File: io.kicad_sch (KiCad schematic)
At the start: 1 part, among them IC24 82C711

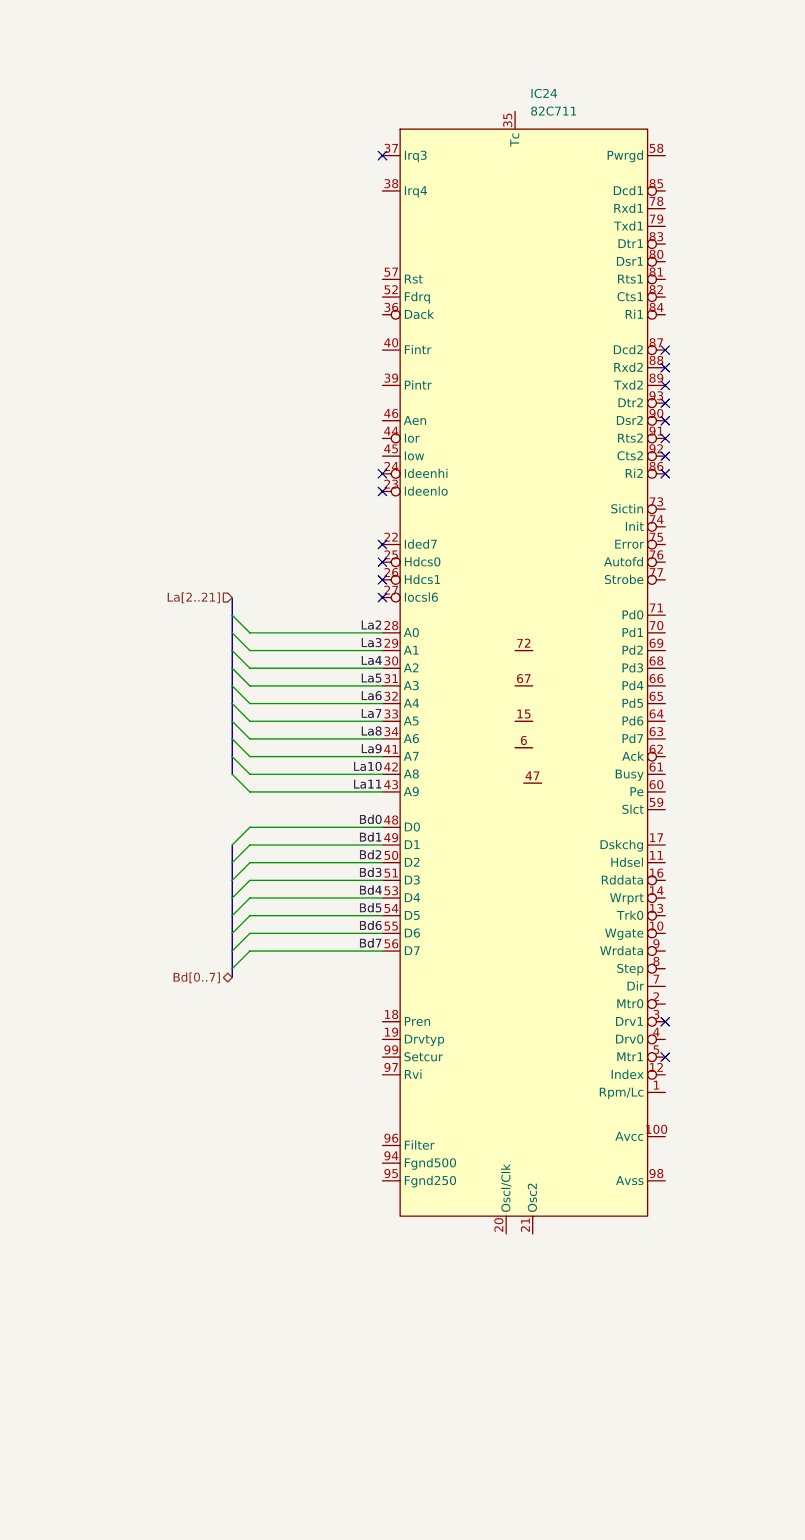
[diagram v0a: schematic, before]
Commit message: add io details
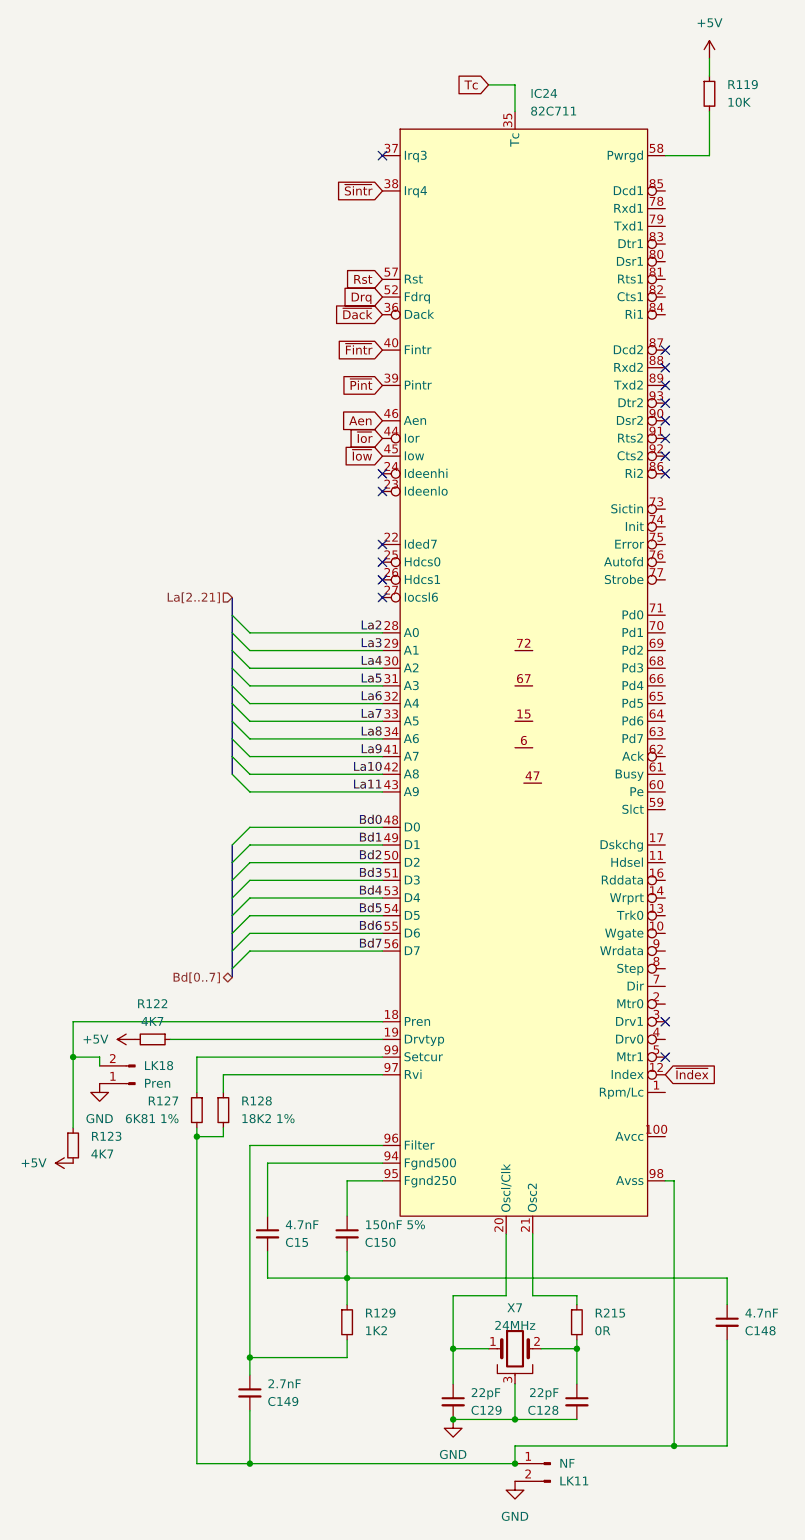
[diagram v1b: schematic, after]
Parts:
- added C128, C129: 22pF, Capacitor_SMD:C_0805_2012Metric, symbol Device:C_Small
- added C148, C15: 4.7nF, Capacitor_THT:C_Rect_L7.0mm_W2.5mm_P5.00mm, symbol Device:C_Small
- added C149: 2.7nF, Capacitor_SMD:C_0805_2012Metric, symbol Device:C_Small
- added C150: 150nF 5%, Capacitor_THT:C_Rect_L7.0mm_W2.5mm_P5.00mm, symbol Device:C_Small
- added LK11: NF, Connector_PinHeader_2.54mm:PinHeader_1x02_P2.54mm_Vertical, symbol Connector:Conn_01x02_Pin
- added LK18: Pren, Connector_PinHeader_2.54mm:PinHeader_1x02_P2.54mm_Vertical, symbol Connector:Conn_01x02_Pin
- added R119: 10K, Resistor_SMD:R_0805_2012Metric, symbol Device:R_Small
- added R122, R123: 4K7, Resistor_SMD:R_0805_2012Metric, symbol Device:R_Small
- added R127: 6K81 1%, Resistor_SMD:R_0805_2012Metric, symbol Device:R_Small
- added R128: 18K2 1%, Resistor_SMD:R_0805_2012Metric, symbol Device:R_Small
- added R129: 1K2, Resistor_SMD:R_0805_2012Metric, symbol Device:R_Small
- added R215: 0R, Resistor_SMD:R_0805_2012Metric, symbol Device:R_Small
- added X7: 24MHz, Crystal:Crystal_HC50_Horizontal_1EP_style2, symbol Device:Crystal_GND3
- IC24: footprint Package_QFP:TQFP-100_14x14mm_P0.5mm -> Package_QFP:PQFP-100_14x20mm_P0.65mm
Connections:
- net ~{Index}: now reaches IC24.12 (Index)
- net at IC24.18 (Pren): now also LK18.2 (Pin_2), R123.1
- net at IC24.19 (Drvtyp): now also R122.1
- net at IC24.20 (Oscl/Clk): now also C129.1, X7.1
- net at IC24.21 (Osc2): now also R215.1
- net Tc: now reaches IC24.35 (Tc)
- net ~{Dack}: now reaches IC24.36 (Dack)
- net ~{Sintr}: now reaches IC24.38 (Irq4)
- net ~{Pint}: now reaches IC24.39 (Pintr)
- net ~{Fintr}: now reaches IC24.40 (Fintr)
- net ~{Ior}: now reaches IC24.44 (Ior)
- net ~{Iow}: now reaches IC24.45 (Iow)
- net Aen: now reaches IC24.46 (Aen)
- net Drq: now reaches IC24.52 (Fdrq)
- net Rst: now reaches IC24.57 (Rst)
- net at IC24.58 (Pwrgd): now also R119.2
- net at IC24.94 (Fgnd500): now also C15.1
- net at IC24.95 (Fgnd250): now also C150.1
- net at IC24.96 (Filter): now also C149.1, R129.2
- net at IC24.97 (Rvi): now also R128.1
- net at IC24.98 (Avss): now also C148.2, C149.2, LK11.1 (Pin_1), R127.2, R128.2
- net at IC24.99 (Setcur): now also R127.1
- new net: C148.1, C15.2, C150.2, R129.1
- new net: C128.1, R215.2, X7.2
- new net +5V: R119.1, R122.2, R123.2
- new net GND: C128.2, C129.2, LK11.2 (Pin_2), LK18.1 (Pin_1), X7.3

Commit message: extend io schematic
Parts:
- added C108, C111, C112, C113, C114, C115, C122, C123, C125, C153, C154, C155, C156: 100pF, Capacitor_SMD:C_0805_2012Metric, symbol Device:C_Small
- added C127, C133, C135, C141, C142, C143, C144, C145: 1nF, Capacitor_SMD:C_0805_2012Metric, symbol Device:C_Small
- added IC16, IC23: MC1489, Package_SO:SOIC-14_3.9x8.7mm_P1.27mm, symbol Acorn:MC1489
- added IC19: MC1488, Package_SO:SOIC-14_3.9x8.7mm_P1.27mm, symbol Acorn:MC1488
- added PL8: Serial, Connector_Dsub:DSUB-9_Male_Horizontal_P2.77x2.84mm_EdgePinOffset9.90mm_Housed_MountingHolesOffset11.32mm, symbol Connector:DE9_Receptacle_MountingHoles
- added R120: 33R, Resistor_SMD:R_0805_2012Metric, symbol Device:R_Small
- added RP8, RP9: 33R, Package_SO:SOIC-16W_5.3x10.2mm_P1.27mm, symbol Device:R_Pack08
- added SK10: Printer, symbol Acorn:DE25_MountingHoles
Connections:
- net GND: now also C108.2, C111.2, C112.2, C113.2, C114.2, C115.2, C122.2, C123.2, C125.2, C127.2, C133.2, C135.2, C141.2, C142.2, C143.2, C144.2, C145.2, C153.2, C154.2, C155.2, C156.2, IC16.7 (GND), IC19.7 (GND), IC23.7 (GND), PL8.0 (PAD), PL8.5
- net at IC24.59 (Slct): now also RP8.16 (R1.2)
- net at IC24.60 (Pe): now also RP8.15 (R2.2)
- net at IC24.61 (Busy): now also RP8.14 (R3.2)
- net at IC24.62 (Ack): now also RP8.13 (R4.2)
- net at IC24.63 (Pd7): now also RP8.12 (R5.2)
- net at IC24.64 (Pd6): now also RP8.11 (R6.2)
- net at IC24.65 (Pd5): now also RP8.10 (R7.2)
- net at IC24.66 (Pd4): now also RP8.9 (R8.2)
- net at IC24.68 (Pd3): now also RP9.16 (R1.2)
- net at IC24.69 (Pd2): now also RP9.15 (R2.2)
- net at IC24.70 (Pd1): now also RP9.14 (R3.2)
- net at IC24.71 (Pd0): now also RP9.12 (R5.2)
- net at IC24.73 (Sictin): now also R120.1
- net at IC24.74 (Init): now also RP9.9 (R8.2)
- net at IC24.75 (Error): now also RP9.13 (R4.2)
- net at IC24.76 (Autofd): now also RP9.10 (R7.2)
- net at IC24.77 (Strobe): now also RP9.11 (R6.2)
- net at IC24.78 (Rxd1): now also IC23.6 (OutputB)
- net at IC24.79 (Txd1): now also IC19.5 (InputB2)
- net at IC24.80 (Dsr1): now also IC16.3 (OutputA)
- net at IC24.81 (Rts1): now also IC19.12 (InputD2)
- net at IC24.82 (Cts1): now also IC16.11 (OutputD)
- net at IC24.83 (Dtr1): now also IC19.9 (InputC2)
- net at IC24.84 (Ri1): now also IC16.8 (OutputC)
- net at IC24.85 (Dcd1): now also IC23.3 (OutputA)
- new net: C112.1, IC16.13 (InputD), PL8.8
- new net: C123.1, IC23.1 (InputA), PL8.1
- new net: C115.1, IC23.4 (InputB), PL8.2
- new net: C113.1, IC19.6 (OutputB), PL8.3
- new net: C111.1, IC19.8 (OutputC), PL8.4
- new net: C122.1, IC16.1 (InputA), PL8.6
- new net: C114.1, IC19.11 (OutputD), PL8.7
- new net: C108.1, IC16.10 (InputC), PL8.9
- new net: C141.1, RP9.1 (R1.1), SK10.5
- new net: C153.1, RP8.4 (R4.1), SK10.10
- new net: C125.1, RP9.6 (R6.1), SK10.1
- new net: C154.1, RP8.3 (R3.1), SK10.11
- new net: C155.1, RP8.2 (R2.1), SK10.12
- new net: C156.1, RP8.1 (R1.1), SK10.13
- new net: C127.1, RP9.5 (R5.1), SK10.2
- new net: C133.1, RP9.3 (R3.1), SK10.3
- new net: C135.1, RP9.2 (R2.1), SK10.4
- new net: C142.1, RP8.8 (R8.1), SK10.6
- new net: C143.1, RP8.7 (R7.1), SK10.7
- new net: C144.1, RP8.6 (R6.1), SK10.8
- new net: C145.1, RP8.5 (R5.1), SK10.9
- no-connect marks 17 -> 32
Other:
- moved on the sheet: C128, C129, C148, C149, C15, C150, IC24, LK11, LK18, R119, R122, R123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

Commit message: progress schematic
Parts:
- added C126, C132, C134, C136: 100pF, Capacitor_SMD:C_0805_2012Metric, symbol Device:C_Small
- added C146: 33nF, Capacitor_SMD:C_0805_2012Metric, symbol Device:C_Small
- added C147, C158: 100nF, Capacitor_SMD:C_0805_2012Metric, symbol Device:C_Small
- added C157: 47uF, Capacitor_THT:CP_Radial_D8.0mm_P5.00mm, symbol Device:C_Polarized_Small
- added D21: BAT, Package_TO_SOT_SMD:SOT-23-3, symbol Device:D_Dual_CommonCathode_AAK
- added L14: 2R2, Acorn:L_Acorn_8x3mm, symbol Device:L_Small
- added PL9: 34WAYBOXPLUG, Connector_IDC:IDC-Header_2x17_P2.54mm_Vertical, symbol Connector_Generic:Conn_02x17_Odd_Even
- added R116, R117, R118, R121, R126, R131, R138, R140, R141: 4K7, Resistor_SMD:R_0805_2012Metric, symbol Device:R_Small
- added R139, R142, R143, R144, R145: 1K, Resistor_SMD:R_0805_2012Metric, symbol Device:R_Small
- SK10: footprint (none) -> Connector_Dsub:DSUB-25_Female_Horizontal_P2.77x2.84mm_EdgePinOffset9.90mm_Housed_MountingHolesOffset11.32mm
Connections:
- net +5V: now also C158.1, L14.2, R138.2, R139.2, R140.2, R141.2, R142.2, R143.2, R144.2, R145.2
- net GND: now also SK10.0, SK10.18, SK10.19, SK10.20, SK10.21, SK10.22, SK10.23, SK10.24, SK10.25, C126.2, C132.2, C134.2, C136.2, C146.2, C147.2, C157.2, C158.2, D21.2 (A), PL9.11 (Pin_11), PL9.13 (Pin_13), PL9.15 (Pin_15), PL9.17 (Pin_17), PL9.19 (Pin_19), PL9.21 (Pin_21), PL9.23 (Pin_23), PL9.25 (Pin_25), PL9.27 (Pin_27), PL9.29 (Pin_29), PL9.3 (Pin_3), PL9.31 (Pin_31), PL9.33 (Pin_33), PL9.5 (Pin_5), PL9.7 (Pin_7), PL9.9 (Pin_9)
- net ~{Index}: now also D21.3 (K), PL9.8 (Pin_8), R139.1
- net at C153.1, RP8.4 (R4.1), SK10.10: now also R126.1
- net at C125.1, RP9.6 (R6.1), SK10.1: now also R116.1
- net at C154.1, RP8.3 (R3.1), SK10.11: now also R131.1
- net at SK10.14: now also RP9.7 (R7.1), C126.1, R117.1
- net at SK10.15: now also RP9.4 (R4.1), C132.1
- net at SK10.16: now also RP9.8 (R8.1), C134.1, R118.1
- net at SK10.17: now also R120.2, C136.1, R121.1
- net Density: now reaches IC24.1 (Rpm/Lc)
- net Density: now also PL9.2 (Pin_2), R138.1
- net ~{Writegate}: now reaches IC24.10 (Wgate)
- net ~{Writegate}: now also PL9.24 (Pin_24)
- net at IC24.100 (Avcc): now also C147.1, L14.1
- net ~{Side1}: now reaches IC24.11 (Hdsel)
- net ~{Side1}: now also PL9.32 (Pin_32)
- net ~{Track00}: now reaches IC24.13 (Trk0)
- net ~{Track00}: now also PL9.26 (Pin_26), R142.1
- net ~{Writeprot}: now reaches IC24.14 (Wrprt)
- net ~{Writeprot}: now also PL9.28 (Pin_28), R143.1
- net ~{Readdata}: now reaches IC24.16 (Rddata)
- net ~{Readdata}: now also PL9.30 (Pin_30), R144.1
- net DC: now reaches IC24.17 (Dskchg)
- net DC: now also PL9.34 (Pin_34), R145.1
- net ~{MotorOn}: now reaches IC24.2 (Mtr0)
- net ~{MotorOn}: now also PL9.16 (Pin_16), R141.1
- net ~{Sel0}: now reaches IC24.4 (Drv0)
- net ~{Sel0}: now also PL9.10 (Pin_10), R140.1
- net ~{Dirin}: now reaches IC24.7 (Dir)
- net ~{Dirin}: now also PL9.18 (Pin_18)
- net ~{Step}: now reaches IC24.8 (Step)
- net ~{Step}: now also PL9.20 (Pin_20)
- net ~{Writedata}: now reaches IC24.9 (Wrdata)
- net ~{Writedata}: now also PL9.22 (Pin_22)
- net +5C: now reaches IC23.14 (VCC)
- net +5C: now also IC16.14 (VCC), IC19.14 (VCC), C146.1, C157.1, R116.2, R117.2, R118.2, R121.2, R126.2, R131.2
- no-connect marks 32 -> 38
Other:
- moved on the sheet: C148, IC16B, IC16E, IC19A, IC19E, IC23C, IC23D, IC23E, R120

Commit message: work on io circuits
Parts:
- added C137: 33nF, Capacitor_SMD:C_0805_2012Metric, symbol Device:C_Small
- added C139: 10uF, Capacitor_THT:CP_Radial_Tantal_D9.0mm_P5.00mm, symbol Device:C_Polarized_Small
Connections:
- net +5V: now also IC24.15, C137.1, C139.1
- net GND: now also C137.2, C139.2

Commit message: more routing
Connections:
- net +5V: now also IC24.72
- net GND: now also IC16.4 (InputB), IC19.2 (InputA), IC23.10 (InputC), IC23.13 (InputD), IC24.67
- net -12V: now reaches IC19.1 (VEE)

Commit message: yet more traces
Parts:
- added RX1: 4k7, Resistor_THT:R_Axial_DIN0204_L3.6mm_D1.6mm_P5.08mm_Horizontal, symbol Device:R_Small
- R127, R128: footprint Resistor_SMD:R_0805_2012Metric -> Resistor_SMD:R_1206_3216Metric
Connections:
- net GND: now also IC24.47, IC24.6
- net ~{Index}: now also RX1.1, RX1.2

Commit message: more analogue video work
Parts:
- added CX2: 68pF, Capacitor_THT:C_Disc_D4.3mm_W1.9mm_P5.00mm, symbol Device:C_Small
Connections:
- net GND: now also D21.1 (A), CX2.2; no longer D21.2 (A)
- net ~{Index}: now also CX2.1
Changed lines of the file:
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@@
 	)
 	(junction
+		(at 142.24 251.46)
+		(diameter 0)
+		(color 0 0 0 0)
+	)
+	(junction
 		(at 270.51 255.27)
 		(diameter 0)
@@
 	(wire
 		(pts
+			(xy 142.24 252.73) (xy 142.24 251.46)
+		)
+		(stroke
+			(width 0)
+			(type default)
+		)
+	)
+	(wire
+		(pts
 			(xy 233.68 64.77) (xy 245.11 64.77)
 		)
@@
 	(wire
 		(pts
+			(xy 153.67 260.35) (xy 130.81 260.35)
+		)
+		(stroke
+			(width 0)
+			(type default)
+		)
+	)
+	(wire
+		(pts
 			(xy 102.87 228.6) (xy 97.79 228.6)
 		)
@@
 	(wire
 		(pts
+			(xy 153.67 242.57) (xy 153.67 260.35)
+		)
+		(stroke
+			(width 0)
+			(type default)
+		)
+	)
+	(wire
+		(pts
 			(xy 168.91 123.19) (xy 168.91 120.65)
 		)
@@
 	(wire
 		(pts
+			(xy 142.24 251.46) (xy 142.24 250.19)
+		)
+		(stroke
+			(width 0)
+			(type default)
+		)
+	)
+	(wire
+		(pts
 			(xy 247.65 133.35) (xy 193.04 133.35)
 		)
@@
 	(wire
 		(pts
+			(xy 138.43 251.46) (xy 142.24 251.46)
+		)
+		(stroke
+			(width 0)
+			(type default)
+		)
+	)
+	(wire
+		(pts
 			(xy 128.27 62.23) (xy 172.72 62.23)
 		)
@@
 	(wire
 		(pts
+			(xy 130.81 251.46) (xy 133.35 251.46)
+		)
+		(stroke
+			(width 0)
+			(type default)
+		)
+	)
+	(wire
+		(pts
 			(xy 179.07 273.05) (xy 254 273.05)
 		)
@@
 	(wire
 		(pts
+			(xy 130.81 260.35) (xy 130.81 251.46)
+		)
+		(stroke
+			(width 0)
+			(type default)
+		)
+	)
+	(wire
+		(pts
 			(xy 325.12 137.16) (xy 328.93 137.16)
 		)
@@
 		(lib_id "Device:D_Dual_CommonCathode_AAK")
 		(at 142.24 242.57 90)
-		(mirror x)
 		(unit 1)
 		(exclude_from_sim no)
@@
 	)
 	(symbol
+		(lib_id "Device:C_Small")
+		(at 135.89 251.46 90)
+		(mirror x)
+		(unit 1)
+		(exclude_from_sim no)
+		(in_bom yes)
+		(on_board yes)
+		(dnp no)
+		(property "Reference" "CX2"
+			(at 137.1665 248.92 0)
+			(effects
+				(font
+					(size 1.27 1.27)
+				)
+				(justify right)
+			)
+		)
+		(property "Value" "68pF"
+			(at 134.6265 248.92 0)
+			(effects
+				(font
+					(size 1.27 1.27)
+				)
+				(justify right)
+			)
+		)
+		(property "Footprint" "Capacitor_THT:C_Disc_D4.3mm_W1.9mm_P5.00mm"
+			(at 135.89 251.46 0)
+			(effects
+				(font
+					(size 1.27 1.27)
+				)
+				(hide yes)
+			)
+		)
+		(property "Datasheet" "~"
+			(at 135.89 251.46 0)
+			(effects
+				(font
+					(size 1.27 1.27)
+				)
+				(hide yes)
+			)
+		)
+		(property "Description" "Unpolarized capacitor, small symbol"
+			(at 135.89 251.46 0)
+			(effects
+				(font
+					(size 1.27 1.27)
+				)
+				(hide yes)
+			)
+		)
+		(pin "1"
+		)
+		(pin "2"
+		)
+		(instances
+			(project "Acorn-A3010"
+				(path "/999882f3-94f8-4a89-9093-27a47d0cb289/b04534ef-c242-4ca8-9b8d-9d4b3e26f2f3"
+					(reference "CX2")
+					(unit 1)
+				)
+			)
+		)
+	)
+	(symbol
 		(lib_id "Acorn:MC1488")
 		(at 207.01 57.15 0)
@@
 	(symbol
 		(lib_id "power:GND")
-		(at 142.24 250.19 0)
+		(at 142.24 252.73 0)
 		(unit 1)
 		(exclude_from_sim no)
@@
 		(fields_autoplaced yes)
 		(property "Reference" "#PWR0154"
-			(at 142.24 256.54 0)
+			(at 142.24 259.08 0)
 			(effects
 				(font
@@
 		)
 		(property "Value" "GND"
-			(at 142.24 255.27 0)
+			(at 142.24 257.81 0)
 			(effects
 				(font
@@
 		)
 		(property "Footprint" ""
-			(at 142.24 250.19 0)
+			(at 142.24 252.73 0)
 			(effects
 				(font
@@
 		)
 		(property "Datasheet" ""
-			(at 142.24 250.19 0)
+			(at 142.24 252.73 0)
 			(effects
 				(font
@@
 		)
 		(property "Description" "Power symbol creates a global label with name \"GND\" , ground"
-			(at 142.24 250.19 0)
+			(at 142.24 252.73 0)
 			(effects
 				(font
